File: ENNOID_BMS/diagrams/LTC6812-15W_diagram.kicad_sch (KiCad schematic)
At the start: 20 parts, among them Q1 NMOS, Q2 TSM2323, Q3 NMOS

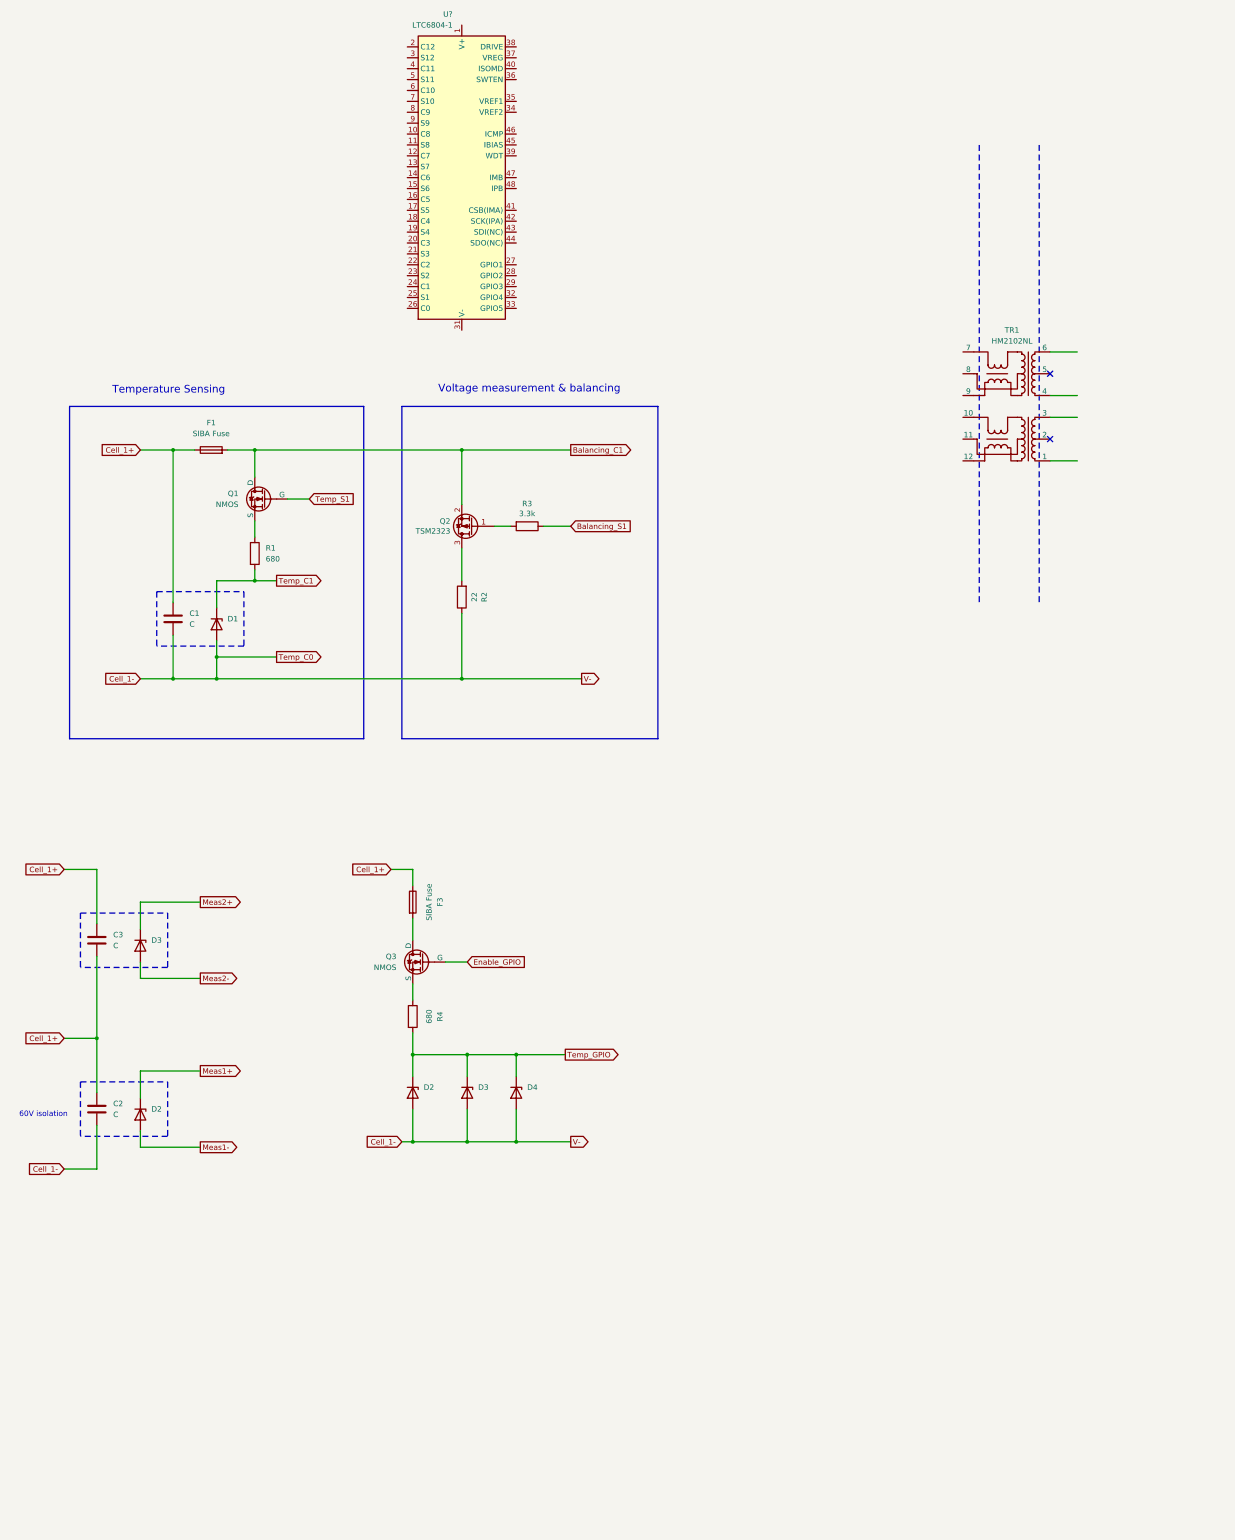
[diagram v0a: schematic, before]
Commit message: Slave with SMD and no other fuses
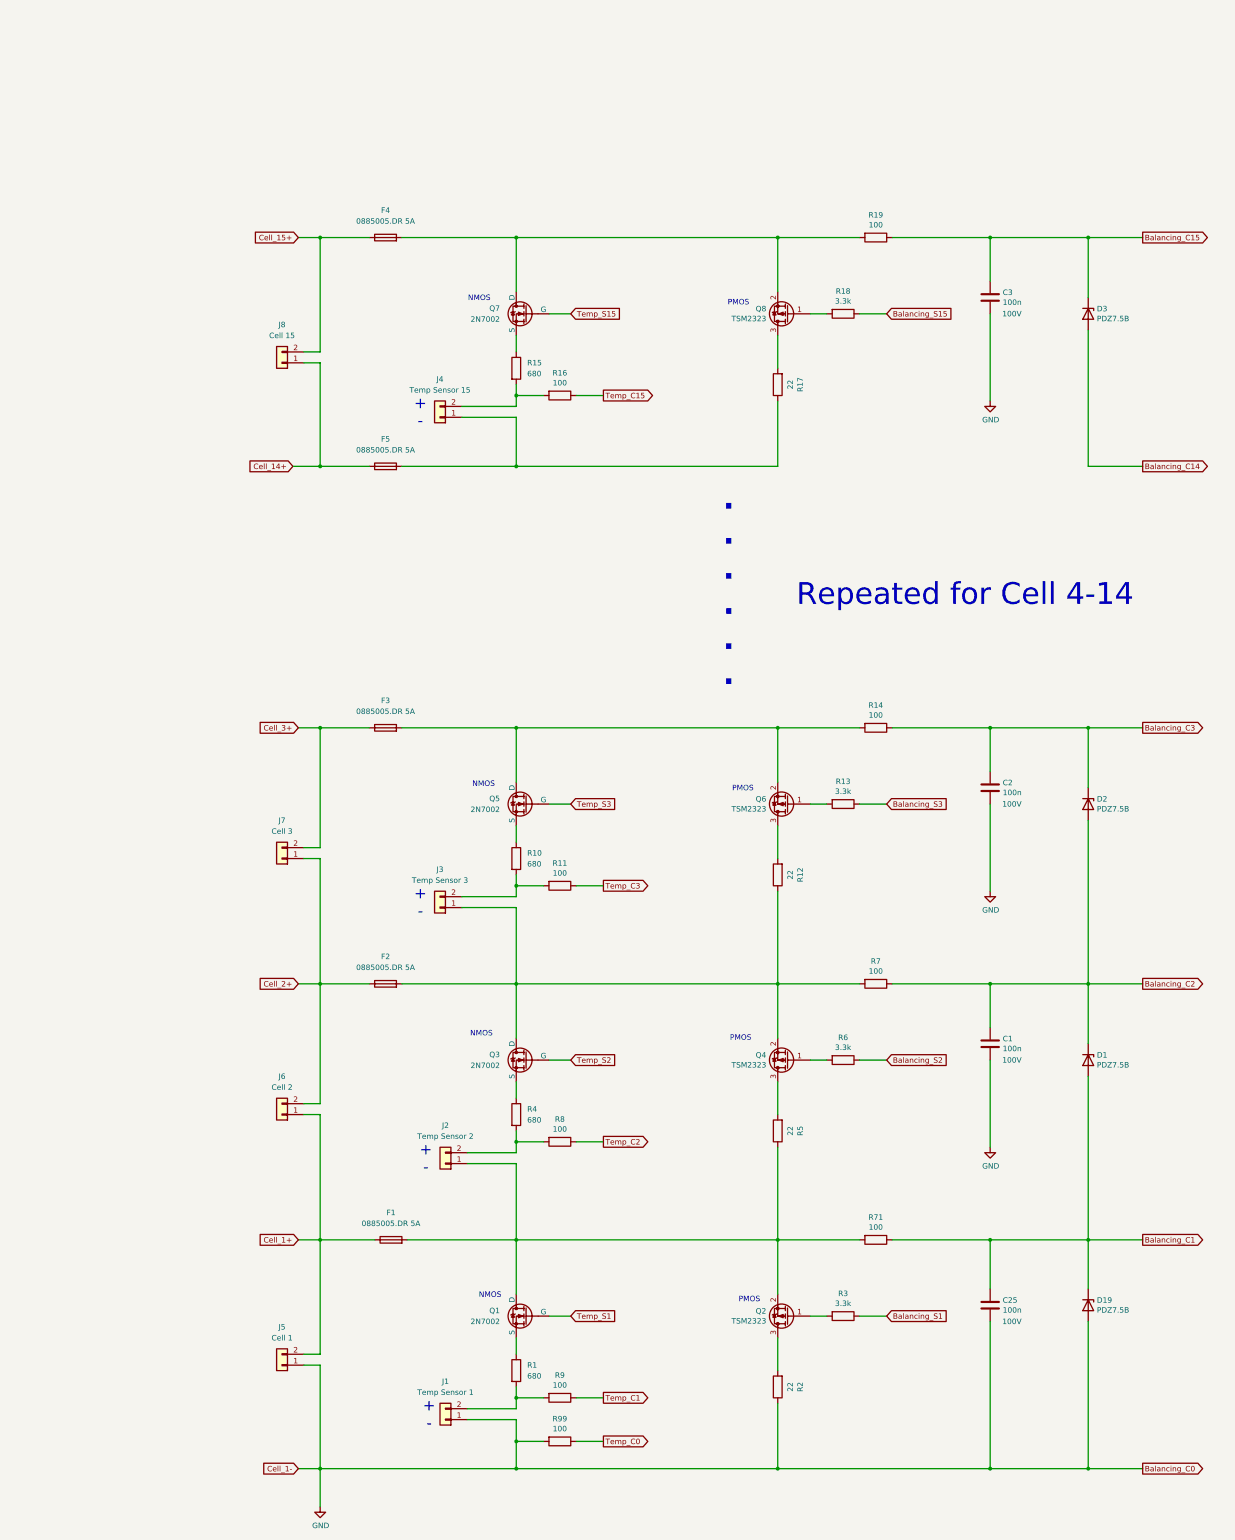
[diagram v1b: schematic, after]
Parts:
- removed D1, D2 (x2), D3 (x2), D4: BZM55Cxx, Diode_SMD:D_MicroMELF, symbol Diode:BZM55Cxx
- removed TR1: HM2102NL, ENNOID:HM2102NL, symbol ENNOID:HM2102NL
- removed U?: LTC6804-1, Package_SO:SSOP-48_5.3x12.8mm_P0.5mm, symbol Battery_Management:LTC6804-1
- added C25: 100n, Capacitor_SMD:C_0603_1608Metric, symbol Device:C
- added D1, D19, D2, D3: PDZ7.5B, Diode_SMD:D_SOD-323, symbol Device:D_Zener
- added F2, F4, F5: 0885005.DR 5A, ENNOID:FUSC10948X488N, symbol Device:Fuse
- added J1: Temp Sensor 1, symbol Connector_Generic:Conn_01x02
- added J2: Temp Sensor 2, symbol Connector_Generic:Conn_01x02
- added J3: Temp Sensor 3, symbol Connector_Generic:Conn_01x02
- added J4: Temp Sensor 15, symbol Connector_Generic:Conn_01x02
- added J5: Cell 1, symbol Connector_Generic:Conn_01x02
- added J6: Cell 2, symbol Connector_Generic:Conn_01x02
- added J7: Cell 3, symbol Connector_Generic:Conn_01x02
- added J8: Cell 15, symbol Connector_Generic:Conn_01x02
- added Q4, Q6, Q8: TSM2323, Package_TO_SOT_SMD:SOT-23, symbol Device:Q_PMOS_GSD
- added Q5, Q7: 2N7002, symbol Simulation_SPICE:NMOS
- added R10, R15: 680, symbol Device:R
- added R11, R14, R16, R19, R7, R71, R8, R9, R99: 100, Resistor_SMD:R_0603_1608Metric, symbol Device:R
- added R12, R17, R5: 22, Resistor_SMD:R_2512_6332Metric, symbol Device:R
- added R13, R18, R6: 3.3k, Resistor_SMD:R_0603_1608Metric, symbol Device:R
- C1, C2, C3: value C -> 100n; footprint (none) -> Capacitor_SMD:C_0603_1608Metric; Part Number (none) -> GRM188R72A104KA35D; Voltage (none) -> 100V
- F1, F3: value SIBA Fuse -> 0885005.DR 5A; footprint (none) -> ENNOID:FUSC10948X488N; Part Number (none) -> 0885005.DR
- Q1, Q3: value NMOS -> 2N7002
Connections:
- net Balancing_C1: now also C25.2, D1.2 (A), D19.1 (K), R71.1; no longer F1.2, Q1.1 (D), Q2.2 (S)
- net Cell_1+: now also J5.2 (Pin_2), J6.1 (Pin_1); no longer C1.1, C2.1, C3.1, C3.2, F3.1
- net Temp_C1: now also R9.1; no longer R1.2
- net at F3.2: now also Q5.1 (D), Q6.2 (S), R14.2; no longer Q3.1 (D)
- removed net Cell_1-: C1.2, C2.2, R2.1
- net Enable_GPIO renamed Temp_S2
- net Temp_GPIO: no longer names the net of R4.2
- net Temp_GPIO: now also J2.2 (Pin_2), R8.2
- new net: F1.2, J2.1 (Pin_1), Q1.1 (D), Q2.2 (S), R5.1, R71.2
- new net: J1.2 (Pin_2), R1.2, R9.2
- new net: Q7.3 (S), R15.1
- new net: J4.2 (Pin_2), R15.2, R16.2
- new net: F2.2, J3.1 (Pin_1), Q3.1 (D), Q4.2 (S), R12.1, R7.2
- new net: Q6.3 (D), R12.2
- new net: Q4.1 (G), R6.2
- new net: F4.2, Q7.1 (D), Q8.2 (S), R19.2
- new net: F5.2, J4.1 (Pin_1), R17.1
- new net: Q6.1 (G), R13.2
- new net: J3.2 (Pin_2), R10.2, R11.2
- new net: Q8.1 (G), R18.2
- new net: Q4.3 (D), R5.2
- new net: Q5.3 (S), R10.1
- new net: Q8.3 (D), R17.2
- new net Balancing_C14: D3.2 (A)
- new net Balancing_C15: C3.2, D3.1 (K), R19.1
- new net Balancing_C2: C1.2, D1.1 (K), D2.2 (A), R7.1
- new net Balancing_C3: C2.2, D2.1 (K), R14.1
- new net Balancing_S15: R18.1
- new net Balancing_S2: R6.1
- new net Balancing_S3: R13.1
- new net Cell_14+: F5.1, J8.1 (Pin_1)
- new net Cell_15+: F4.1, J8.2 (Pin_2)
- new net Cell_2+: F2.1, J6.2 (Pin_2), J7.1 (Pin_1)
- new net Cell_3+: F3.1, J7.2 (Pin_2)
- new net GND: C1.1, C2.1, C25.1, C3.1, D19.2 (A), J1.1 (Pin_1), J5.1 (Pin_1), R2.1, R99.2
- new net Temp_C0: R99.1
- new net Temp_C15: R16.1
- new net Temp_C2: R8.1
- new net Temp_C3: R11.1
- new net Temp_S15: Q7.2 (G)
- new net Temp_S3: Q5.2 (G)
- no-connect marks 2 -> 0
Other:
- note added: "+ -"
- note added: ". . . . . ."
- note added: "NMOS"
- note added: "PMOS"
- note added: "Repeated for Cell 4-14"
- note removed: "60V isolation"
- note removed: "Temperature Sensing"
- note removed: "Voltage measurement & balancing"
- moved on the sheet: Q1, Q2, R1, R2, R3
